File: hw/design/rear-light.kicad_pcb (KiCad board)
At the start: 2 copper layers, 65.8 x 21.8 mm, 109 parts, among them J1 Conn_ARM_SWD_TagConnect_TC203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, Q501 2N7002, Q502 2N7002, Q503 2N7002, Q601 2N7002, U300 MCP2021A-330E/SN, U400 ATSAMD21E18A-A, U500 TLD2331-3EP, U600 TLD2132-1EP, U700 BMA456

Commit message: Gen1.0 design finalization (#1)
* Final layout for Gen1.0, PCB has been ordered
* Design documentation is mostly done
* Schematic has been completed
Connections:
- net Net-(D506-A) renamed /TLD2331_OUT1a
- net Net-(D511-A) renamed /TLD2331_OUT3a
- net Net-(D511-K) renamed /TLD2331_OUT3b
- net Net-(D512-K) renamed /TLD2331_OUT3c
- net Net-(D516-A) renamed /TLD2331_OUT2a
- net Net-(D516-K) renamed /TLD2331_OUT2b
- net Net-(D517-K) renamed /TLD2331_OUT2c
- net Net-(D604-A) renamed /TLD2132_OUTa
- net Net-(D604-K) renamed /TLD2132_OUTb
- net Net-(D605-K) renamed /TLD2132_OUTc
- net Net-(Q501-G) renamed /M05_INSET1a
- net Net-(Q502-G) renamed /M05_INSET2a
- net Net-(Q503-G) renamed /M05_INSET3a
- net Net-(Q601-G) renamed /M06_INSETa
- net Net-(U500-IN_SET1) renamed /TLD2331_INSET1a
- net Net-(U500-IN_SET2) renamed /TLD2331_INSET2a
- net Net-(U500-IN_SET3) renamed /TLD2331_INSET3a
- net Net-(U600-IN_SET) renamed /TLD2132_INSETa
- D506 pad 1: Net-(D506-K) -> /TLD2331_OUT1c
- D507 pad 1: Net-(D507-K) -> /TLD2331_OUT1c
- D507 pad 2: Net-(D506-K) -> /TLD2331_OUT1c
- D508 pad 2: Net-(D507-K) -> /TLD2331_OUT1c
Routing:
- net /TLD2331_OUT1c: track 0.00 -> 30.8 mm
- net Net-(D507-K): track 15.5 -> 0.00 mm
- net Net-(D506-K): track 15.3 -> 0.00 mm

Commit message: Initial design Schematic is mostly complete
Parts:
- removed C302: 220p, Capacitor_SMD:C_0603_1608Metric
- removed C303, C304, C407, C410: 10u, Capacitor_SMD:C_0805_2012Metric
- removed C306, C408, C411, C414, C504, C602: 220n, Capacitor_SMD:C_0402_1005Metric
- removed C412: 2.2u, Capacitor_SMD:C_0805_2012Metric
- removed C509, C514, C519, C525, C607: 10n, Capacitor_SMD:C_0402_1005Metric
- removed C527, C613: 2.2n, Capacitor_SMD:C_0402_1005Metric
- removed D201, D301: SMF33CA-DIO, Diode_SMD:D_SMF
- removed D506, D507, D508, D511, D512, D513, D516, D517, D518, D604, D605, D606: LED, LED_SMD:LED_0805_2012Metric
- removed L409: 10uH, Inductor_SMD:L_0805_2012Metric
- removed Q501, Q502, Q503: 2N7002, Package_TO_SOT_SMD:SOT-23
- removed R305, R307, R413, R529, R531, R533, R536, R538, R540, R615, R619, R620, R621: 10k, Resistor_SMD:R_0402_1005Metric
- removed R403: 1k, Resistor_SMD:R_0402_1005Metric
- removed R505, R510, R515, R603: 0, Resistor_SMD:R_0603_1608Metric
- removed R520, R521, R522, R608: 18.3k, Resistor_SMD:R_0402_1005Metric
- removed R523, R609: 20k, Resistor_SMD:R_0402_1005Metric
- removed R524, R526, R528, R612, R614: 0, Resistor_SMD:R_0402_1005Metric
- removed R532: 47k, Resistor_SMD:R_0402_1005Metric
- removed R537, R539, R541, R617: 220, Resistor_SMD:R_0402_1005Metric
- removed TP1, TP10, TP11, TP12, TP13, TP14, TP15, TP16, TP2, TP20, TP21, TP22, TP23, TP3, TP4, TP5, TP6, TP7, TP8, TP9: ~, TestPoint:TestPoint_Pad_1.0x1.0mm
- removed U100: ~, Connector_JST:JST_JWPF_B04B-JWPF-SK-R_1x04_P2.00mm_Vertical
- removed U300: MCP2021A-330E/SN, Package_SO:SOIC-8_3.9x4.9mm_P1.27mm
- removed U400: ATSAMD21E18A-A, Package_QFP:TQFP-32_7x7mm_P0.8mm
- removed U500: TLD2331-3EP, Package_SO:Infineon_PG-TSDSO-14-22
- removed U600: TLD2132-1EP, Package_SO:Infineon_PG-TSDSO-14-22
- added C1: 100n, Capacitor_SMD:C_0402_1005Metric, B.Cu at (64.2, 54.5)
- added C10: 10u, Capacitor_SMD:C_0805_2012Metric, B.Cu at (76.3, 61.1)
- added C11: 22u, Capacitor_SMD:C_0805_2012Metric, B.Cu at (76.3, 64.1)
- added C12: 10u, Capacitor_SMD:C_0402_1005Metric, B.Cu at (61.4, 54.5)
- added C13: 100n, Capacitor_SMD:C_0402_1005Metric, B.Cu at (61.4, 56.5)
- added C14: 10u, Capacitor_SMD:C_0402_1005Metric, B.Cu at (61.4, 58.5)
- added C15: 100n, Capacitor_SMD:C_0402_1005Metric, B.Cu at (58.5, 54.5)
- added C16: 1u, Capacitor_SMD:C_0402_1005Metric, B.Cu at (58.5, 56.5)
- added C17: 100n, Capacitor_SMD:C_0402_1005Metric, B.Cu at (58.5, 58.5)
- added C18: 100n, Capacitor_SMD:C_0402_1005Metric, F.Cu at (137.6, 49.3)
- added C19: 100n, Capacitor_SMD:C_0402_1005Metric, F.Cu at (137.6, 51.2)
- added C2: 100u, Capacitor_SMD:CP_Elec_6.3x5.7, B.Cu at (83.4, 68.4)
- added C20: 100p, Capacitor_SMD:C_0402_1005Metric, F.Cu at (137.6, 53.2)
- added C21: 100n, Capacitor_SMD:C_0603_1608Metric, F.Cu at (146.8, 53.1)
- added C22: 10u, Capacitor_SMD:C_0805_2012Metric, F.Cu at (147.0, 50.3)
- added C23: 10n, Capacitor_SMD:C_0402_1005Metric, F.Cu at (137.6, 55.2)
- added C24: 10n, Capacitor_SMD:C_0402_1005Metric, F.Cu at (137.6, 57.1)
- added C25: 10n, Capacitor_SMD:C_0402_1005Metric, F.Cu at (140.5, 45.3)
- added C26: 10n, Capacitor_SMD:C_0402_1005Metric, F.Cu at (140.5, 47.3)
- added C27: 10n, Capacitor_SMD:C_0402_1005Metric, F.Cu at (140.5, 49.3)
- added C28: 10n, Capacitor_SMD:C_0402_1005Metric, F.Cu at (140.5, 51.2)
- added C29: 10n, Capacitor_SMD:C_0402_1005Metric, F.Cu at (140.5, 53.2)
- added C3: 2.2u, Capacitor_SMD:C_0805_2012Metric, B.Cu at (76.3, 55.0)
- added C30: 10n, Capacitor_SMD:C_0402_1005Metric, F.Cu at (140.5, 55.2)
- added C31: 10n, Capacitor_SMD:C_0402_1005Metric, F.Cu at (140.5, 57.1)
- added C32: 10n, Capacitor_SMD:C_0402_1005Metric, F.Cu at (143.3, 45.3)
- added C33: 10n, Capacitor_SMD:C_0402_1005Metric, F.Cu at (143.3, 47.3)
- added C34: 10n, Capacitor_SMD:C_0402_1005Metric, F.Cu at (143.3, 49.3)
- added C35: 10u, Capacitor_SMD:C_0402_1005Metric, F.Cu at (143.3, 51.2)
- added C36: 10u, Capacitor_SMD:C_0402_1005Metric, F.Cu at (143.3, 53.2)
- added C4: 220p, Capacitor_SMD:C_0603_1608Metric, B.Cu at (64.9, 61.2)
- added C5: 22n, Capacitor_SMD:C_0603_1608Metric, B.Cu at (64.9, 63.8)
- added C6: 100n, Capacitor_SMD:C_0402_1005Metric, F.Cu at (137.6, 45.3)
- added C7: 10n, Capacitor_SMD:C_0402_1005Metric, B.Cu at (64.2, 56.5)
- added C8: 100p, Capacitor_SMD:C_0402_1005Metric, F.Cu at (137.6, 47.3)
- added C9: 100n, Capacitor_SMD:C_0402_1005Metric, B.Cu at (64.2, 58.5)
- added D1: BAS3005B02, Diode_SMD:D_SOD-523, B.Cu at (61.0, 61.2)
- added D10: LY E6SF-ABCA-36-3B5A-50, LED_SMD:LED_Cree-PLCC4_2x2mm_CW, F.Cu at (125.0, 49.9)
- added D11: LY E6SF-ABCA-36-3B5A-50, LED_SMD:LED_Cree-PLCC4_2x2mm_CW, F.Cu at (129.5, 38.3)
- added D12: LY E6SF-ABCA-36-3B5A-50, LED_SMD:LED_Cree-PLCC4_2x2mm_CW, F.Cu at (129.5, 42.2)
- added D13: LY E6SF-ABCA-36-3B5A-50, LED_SMD:LED_Cree-PLCC4_2x2mm_CW, F.Cu at (129.5, 46.0)
- added D14: LY E6SF-ABCA-36-3B5A-50, LED_SMD:LED_Cree-PLCC4_2x2mm_CW, F.Cu at (129.5, 49.9)
- added D15: LY E6SF-ABCA-36-3B5A-50, LED_SMD:LED_Cree-PLCC4_2x2mm_CW, F.Cu at (133.9, 38.3)
- added D16: LY E6SF-ABCA-36-3B5A-50, LED_SMD:LED_Cree-PLCC4_2x2mm_CW, F.Cu at (133.9, 42.2)
- added D17: LY E6SF-ABCA-36-3B5A-50, LED_SMD:LED_Cree-PLCC4_2x2mm_CW, F.Cu at (133.9, 46.0)
- added D18: XPEBRO-L1-0000-00C01, LED_SMD:LED_Cree-XP-G, F.Cu at (72.2, 49.3)
- added D2: SS34F-DC, Diode_SMD:D_SMA, B.Cu at (65.4, 49.3)
- added D3: SDT23C15L02, Package_TO_SOT_SMD:SOT-23, B.Cu at (59.0, 44.2)
- added D5: MM5Z3V6T1G, Diode_SMD:D_SOD-523, B.Cu at (61.0, 66.1)
- added D6: LY E6SF-ABCA-36-3B5A-50, LED_SMD:LED_Cree-PLCC4_2x2mm_CW, F.Cu at (59.7, 37.9)
- added D7: LY E6SF-ABCA-36-3B5A-50, LED_SMD:LED_Cree-PLCC4_2x2mm_CW, F.Cu at (125.0, 38.3)
- added D8: LY E6SF-ABCA-36-3B5A-50, LED_SMD:LED_Cree-PLCC4_2x2mm_CW, F.Cu at (125.0, 42.2)
- added D9: LY E6SF-ABCA-36-3B5A-50, LED_SMD:LED_Cree-PLCC4_2x2mm_CW, F.Cu at (125.0, 46.0)
- added J3: Conn_ARM_SWD_TagConnect_TC2030-NL, Connector:Tag-Connect_TC2030-IDC-NL_2x03_P1.27mm_Vertical, B.Cu at (65.5, 44.5)
- added L2: 2.2u, Inductor_SMD:L_Coilcraft_LPS3010, B.Cu at (59.0, 49.3)
- added L3: 10uH, Inductor_SMD:L_0603_1608Metric, B.Cu at (64.9, 68.8)
- added Q200: SIA469DJ-T1-GE3, Package_TO_SOT_SMD:Vishay_PowerPAK_SC70-6L_Single, F.Cu at (146.8, 38.2)
- added R1: 10k, Resistor_SMD:R_0402_1005Metric, B.Cu at (85.8, 54.5)
- added R10: 0, Resistor_SMD:R_0402_1005Metric, B.Cu at (82.9, 58.5)
- added R11: 20k, Resistor_SMD:R_0402_1005Metric, B.Cu at (82.9, 60.5)
- added R12: 4.7k, Resistor_SMD:R_0402_1005Metric, B.Cu at (82.9, 62.5)
- added R13: 1k, Resistor_SMD:R_0402_1005Metric, B.Cu at (82.9, 64.5)
- added R14: 47k, Resistor_SMD:R_0402_1005Metric, B.Cu at (80.0, 54.5)
- added R15: 4.7k, Resistor_SMD:R_0402_1005Metric, B.Cu at (80.0, 56.5)
- added R16: 10k, Resistor_SMD:R_0402_1005Metric, B.Cu at (80.0, 58.5)
- added R17: 4.7k, Resistor_SMD:R_0402_1005Metric, B.Cu at (81.2, 39.7)
- added R18: 0, Resistor_SMD:R_0603_1608Metric, F.Cu at (146.8, 55.6)
- added R19: 10k, Resistor_SMD:R_0402_1005Metric, F.Cu at (137.6, 37.4)
- added R2: 10k, Resistor_SMD:R_0402_1005Metric, B.Cu at (85.8, 56.5)
- added R20: 0, Resistor_SMD:R_0402_1005Metric, F.Cu at (137.6, 39.4)
- added R200: 47k, Resistor_SMD:R_0402_1005Metric, F.Cu at (143.4, 39.4)
- added R201: 47k, Resistor_SMD:R_0402_1005Metric, F.Cu at (143.4, 41.4)
- added R21: 1k, Resistor_SMD:R_0402_1005Metric, F.Cu at (137.6, 41.4)
- added R22: 4.7k, Resistor_SMD:R_0402_1005Metric, F.Cu at (137.6, 43.3)
- added R23: 4.7k, Resistor_SMD:R_0402_1005Metric, F.Cu at (140.5, 37.4)
- added R24: 1k, Resistor_SMD:R_0402_1005Metric, F.Cu at (140.5, 39.4)
- added R25: 10k, Resistor_SMD:R_0402_1005Metric, F.Cu at (140.5, 41.4)
- added R26: 4.7k, Resistor_SMD:R_0402_1005Metric, F.Cu at (140.5, 43.3)
- added R27: 4.7k, Resistor_SMD:R_0402_1005Metric, F.Cu at (143.4, 37.4)
- added R3: 47k, Resistor_SMD:R_0402_1005Metric, B.Cu at (85.8, 58.5)
- added R4: 10k, Resistor_SMD:R_0402_1005Metric, B.Cu at (85.8, 60.5)
- added R5: 10k, Resistor_SMD:R_0402_1005Metric, B.Cu at (85.8, 62.5)
- added R6: 10k, Resistor_SMD:R_0402_1005Metric, B.Cu at (85.8, 64.5)
- added R7: 1k, Resistor_SMD:R_0402_1005Metric, B.Cu at (82.9, 54.5)
- added R8: 520m, Resistor_SMD:R_1206_3216Metric, B.Cu at (71.3, 68.9)
- added R9: 4.7k, Resistor_SMD:R_0402_1005Metric, B.Cu at (82.9, 56.5)
- added TH1: ERT-J0ER103J, Resistor_SMD:R_0402_1005Metric, F.Cu at (143.4, 43.3)
- added U1: ILD8150, Package_SO:Infineon_PG-DSO-8-27_3.9x4.9mm_EP2.65x3mm, B.Cu at (69.9, 56.8)
- added U2: MCP2003BT-E/MC, Package_DFN_QFN:DFN-8-1EP_3x2mm_P0.5mm_EP1.7x1.4mm, B.Cu at (71.5, 72.3)
- added U3: TPS629210DRLR, Package_TO_SOT_SMD:SOT-583-8, B.Cu at (76.7, 67.4)
- added U4: ~, Connector_JST:JST_JWPF_B03B-JWPF-SK-R_1x03_P2.00mm_Vertical, F.Cu at (70.4, 95.5)
- added U5: ATSAMD21E18A-MUT, Package_DFN_QFN:VQFN-32-1EP_5x5mm_P0.5mm_EP3.5x3.5mm, B.Cu at (70.5, 63.6)
- added U6: TLD7002-16ES, libs:SOP65P600X115-25N, B.Cu at (80.6, 46.9)
- added U8: XM125, libs:XM125_ACC-M, F.Cu at (72.3, 81.9)
- added U9: AP2127N-1.8, Package_TO_SOT_SMD:SOT-23, F.Cu at (147.2, 46.6)
- D200: value BAS3005B02 -> BZT52C20-TP; footprint Diode_SMD:D_SOD-523 -> Diode_SMD:D_SOD-123; moved to F.Cu
- J1: moved to F.Cu
- moved C611 59.1 mm to (202.8, 60.3)
- moved Q601 59.1 mm to (199.9, 62.8)
- moved R610 59.1 mm to (202.8, 61.6)
- moved R618 59.1 mm to (198.6, 60.1)
- moved C702 58.8 mm to (94.3, 59.6)
- moved C701 58.8 mm to (99.3, 59.0)
- moved U700 58.8 mm to (96.9, 58.7)
- moved D200 47.1 mm to (147.1, 59.8), turned to 0 degrees
- moved J1 36.7 mm to (140.2, 60.7), turned to 0 degrees
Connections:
- C611 pad 1: GND -> unconnected-(C611-Pad1)
- C611 pad 2: /TLD2132_DS -> unconnected-(C611-Pad2)
- D200 pad 1: +BATT -> VS
- D200 pad 2: VS -> Net-(D200-A)
- J1 pad 2: /M05_SWDIO -> /M07_RADAR_SWDIO
- J1 pad 3: /M05_RESET -> /~{M07_RADAR_RST}
- J1 pad 4: /M05_SWCLK -> /M07_RADAR_SWCLK
- Q601 pad 1: /M06_INSETa -> unconnected-(Q601-G-Pad1)
- Q601 pad 2: GND -> unconnected-(Q601-S-Pad2)
- Q601 pad 3: /TLD2132_INSET -> unconnected-(Q601-D-Pad3)
- R610 pad 1: GND -> unconnected-(R610-Pad1)
- R610 pad 2: /TLD2132_DS -> unconnected-(R610-Pad2)
- R618 pad 1: GND -> unconnected-(R618-Pad1)
- R618 pad 2: /M06_INSETa -> unconnected-(R618-Pad2)
- U700 pad 6: /M07_ACCEL_INT2 -> unconnected-(U700-INT2-Pad6)
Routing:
- net +3.3V: track 165.3 -> 0.00 mm, vias 9 -> 0
- net /M03_LINE: track 96.6 -> 0.00 mm, vias 1 -> 0
- net VS: track 86.8 -> 0.00 mm
- net /TLD2331_OUT2: track 58.2 -> 0.00 mm, vias 2 -> 0
- net /M05_ENABLE: track 54.8 -> 0.00 mm, vias 4 -> 0
- net /M06_ENABLE: track 49.5 -> 0.00 mm, vias 2 -> 0
- net /M05_ERROR: track 37.3 -> 0.00 mm, vias 2 -> 0
- net /M06_PWMI: track 31.4 -> 0.00 mm, vias 2 -> 0
- net /TLD2331_OUT1c: track 30.8 -> 0.00 mm
- net /M05_PWMI: track 27.1 -> 0.00 mm, vias 2 -> 0
- net /M06_ERROR: track 26.9 -> 0.00 mm, vias 2 -> 0
- net /M06_INSETa: track 25.6 -> 0.00 mm, vias 2 -> 0
- net /M05_RESET: track 19.8 -> 0.00 mm, vias 2 -> 0
- net /M03_CS: track 18.6 -> 0.00 mm, vias 2 -> 0
- net /TLD2331_OUT2c: track 16.0 -> 0.00 mm
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- removed copper zone on B.Cu, net GND
- removed copper zone on F.Cu, net GND
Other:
- board outline removed

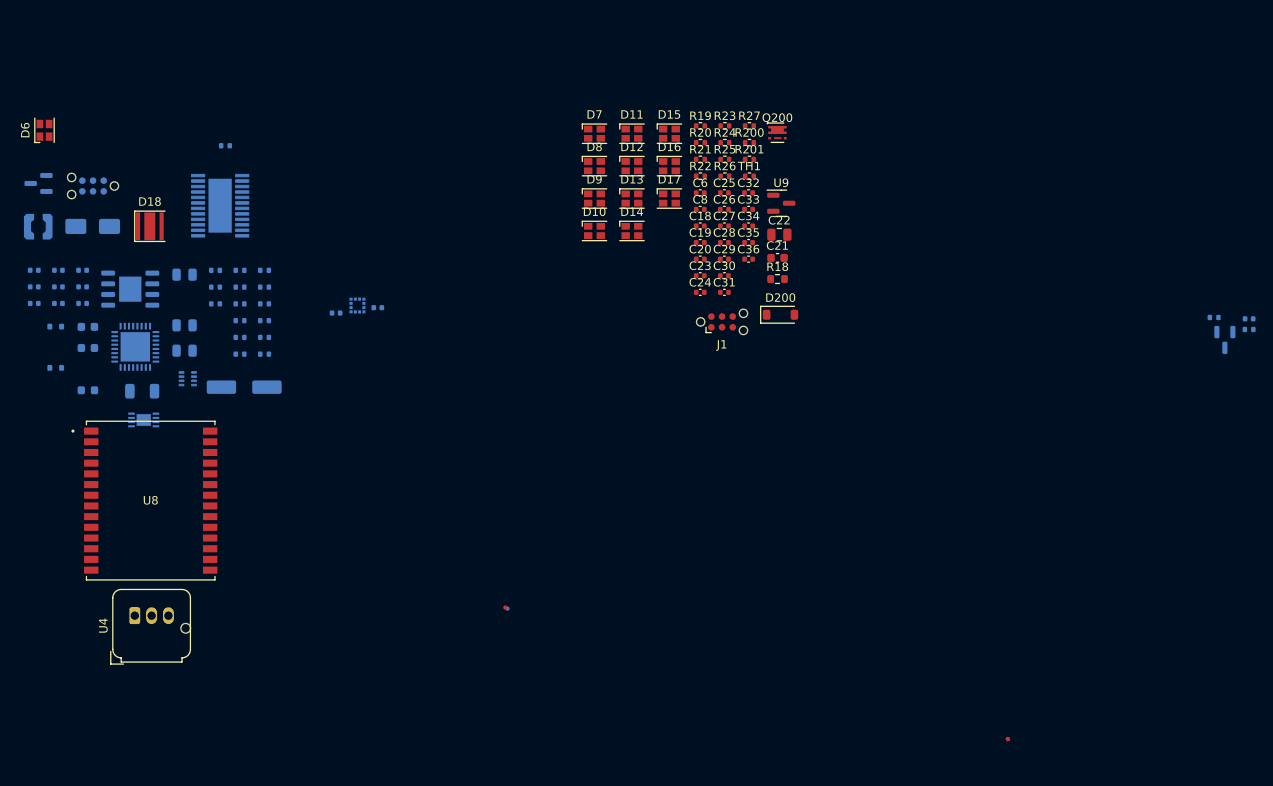
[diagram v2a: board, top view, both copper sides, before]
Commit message: Gen2.0 redesign - DCDC converter for LVIO - Voltage monitoring - Reverse polarity protection is P-FET - MCP2003 as LIN trans. - AL8891 LED driver - XM125 radar
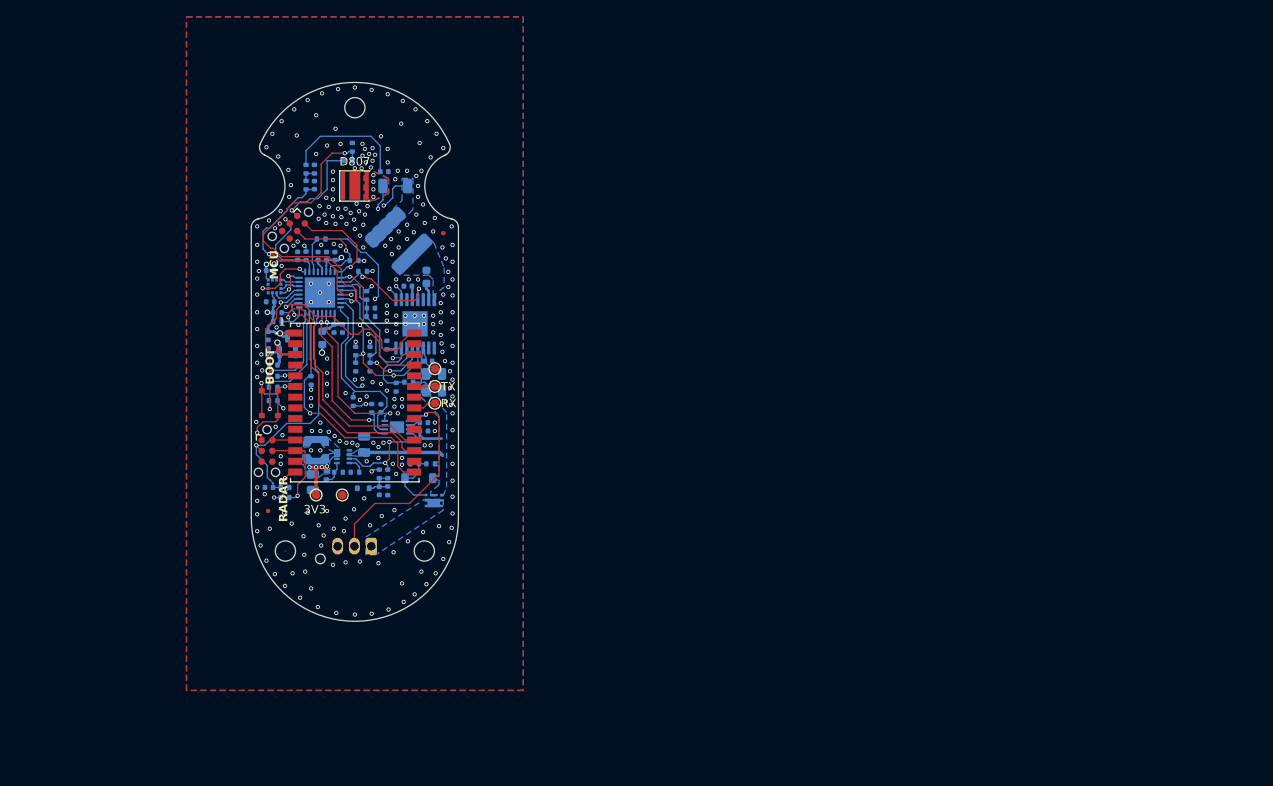
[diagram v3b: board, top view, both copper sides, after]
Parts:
- removed C1, C18: 100n, Capacitor_SMD:C_0402_1005Metric
- removed C2: 100u, Capacitor_SMD:CP_Elec_6.3x5.7
- removed C20: 100p, Capacitor_SMD:C_0402_1005Metric
- removed C21: 100n, Capacitor_SMD:C_0603_1608Metric
- removed C22: 10u, Capacitor_SMD:C_0805_2012Metric
- removed C23, C24, C25, C26, C27, C28, C29, C30, C31, C32, C33, C34, C611, C7: 10n, Capacitor_SMD:C_0402_1005Metric
- removed C3: 2.2u, Capacitor_SMD:C_0805_2012Metric
- removed C4: 220p, Capacitor_SMD:C_0603_1608Metric
- removed C5: 22n, Capacitor_SMD:C_0603_1608Metric
- removed D1: BAS3005B02, Diode_SMD:D_SOD-523
- removed D10, D11, D12, D13, D14, D15, D16, D17, D6, D7, D8, D9: LY E6SF-ABCA-36-3B5A-50, LED_SMD:LED_Cree-PLCC4_2x2mm_CW
- removed D18: XPEBRO-L1-0000-00C01, LED_SMD:LED_Cree-XP-G
- removed D2: SS34F-DC, Diode_SMD:D_SMA
- removed D3: SDT23C15L02, Package_TO_SOT_SMD:SOT-23
- removed Q601: 2N7002, Package_TO_SOT_SMD:SOT-23
- removed R17, R22, R23: 4.7k, Resistor_SMD:R_0402_1005Metric
- removed R18: 0, Resistor_SMD:R_0603_1608Metric
- removed R2, R25, R4, R5, R6, R618: 10k, Resistor_SMD:R_0402_1005Metric
- removed R20, R610: 0, Resistor_SMD:R_0402_1005Metric
- removed R24, R7: 1k, Resistor_SMD:R_0402_1005Metric
- removed R3: 47k, Resistor_SMD:R_0402_1005Metric
- removed R8: 520m, Resistor_SMD:R_1206_3216Metric
- removed TH1: ERT-J0ER103J, Resistor_SMD:R_0402_1005Metric
- removed U1: ILD8150, Package_SO:Infineon_PG-DSO-8-27_3.9x4.9mm_EP2.65x3mm
- removed U5: ATSAMD21E18A-MUT, Package_DFN_QFN:VQFN-32-1EP_5x5mm_P0.5mm_EP3.5x3.5mm
- removed U6: TLD7002-16ES, libs:SOP65P600X115-25N
- added C706: 100n, Capacitor_SMD:C_0402_1005Metric, B.Cu at (86.9, 65.8)
- added C801: 10u, Capacitor_SMD:C_0805_2012Metric, B.Cu at (106.0, 68.8)
- added C802: 2.2u, Capacitor_SMD:C_0805_2012Metric, B.Cu at (106.0, 66.8)
- added C803: 100n, Capacitor_SMD:C_0603_1608Metric, B.Cu at (105.1, 55.3)
- added C806: 100n, Capacitor_SMD:C_0402_1005Metric, B.Cu at (100.1, 42.8)
- added C808: 2.2u, Capacitor_SMD:C_0402_1005Metric, B.Cu at (102.9, 56.4)
- added C816: 10n, Capacitor_SMD:C_0402_1005Metric, B.Cu at (98.5, 59.0)
- added C826: 2.2u, Capacitor_SMD:C_0402_1005Metric, B.Cu at (91.8, 44.4)
- added C827: 100n, Capacitor_SMD:C_0402_1005Metric, B.Cu at (105.3, 65.3)
- added C902: 100n, Capacitor_SMD:C_0402_1005Metric, B.Cu at (99.5, 80.7)
- added D807: XPEBRO-L1-0000-00C01, LED_SMD:LED_Cree-XP-G, F.Cu at (96.6, 44.5)
- added L804: 22u, libs:ASPI-6045, B.Cu at (101.8, 51.0)
- added R709: 10k, Resistor_SMD:R_0402_1005Metric, B.Cu at (88.3, 80.3)
- added R712: 1.5k, Resistor_SMD:R_0402_1005Metric, B.Cu at (86.9, 67.1)
- added R713: 1.5k, Resistor_SMD:R_0402_1005Metric, B.Cu at (86.9, 68.4)
- added R717: 1.5k, Resistor_SMD:R_0402_1005Metric, B.Cu at (86.9, 70.0)
- added R718: 1.5k, Resistor_SMD:R_0402_1005Metric, B.Cu at (92.6, 50.8)
- added R805: 290m, Resistor_SMD:R_1206_3216Metric, B.Cu at (101.4, 44.5)
- added R809: 150k, Resistor_SMD:R_0402_1005Metric, B.Cu at (103.0, 67.8)
- added R810: 100k, Resistor_SMD:R_0402_1005Metric, B.Cu at (101.5, 68.4)
- added R812: 10k, Resistor_SMD:R_0402_1005Metric, B.Cu at (96.7, 64.1)
- added R813: 100k, Resistor_SMD:R_0402_1005Metric, B.Cu at (96.7, 66.0)
- added R814: 47k, Resistor_SMD:R_0402_1005Metric, B.Cu at (97.5, 54.7)
- added R815: 200k, Resistor_SMD:R_0402_1005Metric, B.Cu at (98.0, 57.5)
- added R817: 43k, Resistor_SMD:R_0402_1005Metric, B.Cu at (98.5, 60.0)
- added R818: 47k, Resistor_SMD:R_0402_1005Metric, B.Cu at (98.4, 64.1)
- added R819: 47k, Resistor_SMD:R_0402_1005Metric, B.Cu at (98.4, 66.0)
- added R820: 237k, Resistor_SMD:R_0402_1005Metric, B.Cu at (100.4, 63.4)
- added R822: 10k, Resistor_SMD:R_0402_1005Metric, B.Cu at (96.3, 39.9)
- added R823: 10k, Resistor_SMD:R_0402_1005Metric, B.Cu at (90.8, 42.5)
- added R824: 10k, Resistor_SMD:R_0402_1005Metric, B.Cu at (91.8, 42.5)
- added R825: 10k, Resistor_SMD:R_0402_1005Metric, B.Cu at (90.8, 44.4)
- added R904: 10k, Resistor_SMD:R_0402_1005Metric, B.Cu at (99.5, 78.7)
- added SW716: SW_Push, libs:KMT0, F.Cu at (86.5, 70.3)
- added TH821: ERT-J0ER103J, Resistor_SMD:R_0402_1005Metric, B.Cu at (95.8, 41.5)
- added TP400: TestPoint, TestPoint:TestPoint_Pad_D1.0mm, F.Cu at (92.0, 81.2)
- added TP401: TestPoint, TestPoint:TestPoint_Pad_D1.0mm, F.Cu at (95.1, 81.2)
- added TP700: TestPoint, TestPoint:TestPoint_Pad_D1.0mm, F.Cu at (106.1, 70.3)
- added TP701: TestPoint, TestPoint:TestPoint_Pad_D1.0mm, F.Cu at (106.1, 68.3)
- added TP702: TestPoint, TestPoint:TestPoint_Pad_D1.0mm, F.Cu at (106.1, 66.2)
- added U500: ATSAMD21E18A-M, Package_DFN_QFN:QFN-32-1EP_5x5mm_P0.5mm_EP3.6x3.6mm, B.Cu at (92.4, 57.2)
- added U800: AL8891, Package_SO:TSSOP-16-1EP_4.4x5mm_P0.65mm_EP3x3mm, B.Cu at (103.7, 60.9)
- C302: renamed from C19; moved to B.Cu
- C304: renamed from C8; moved to B.Cu
- C602: renamed from C701; value 220n -> 100n
- C603: renamed from C702; value 220n -> 100n
- C702: renamed from C35; moved to B.Cu
- C703: renamed from C36; moved to B.Cu
- C710: renamed from C6; moved to B.Cu
- D203: renamed from D200; moved to B.Cu
- J501: renamed from J3; moved to F.Cu
- Q200: moved to B.Cu
- R1: value 10k -> 4.7k
- R201: renamed from R200; value 47k -> 820k; moved to B.Cu
- R202: renamed from R201; value 47k -> 680k; moved to B.Cu
- R704: renamed from R21; moved to B.Cu
- R708: renamed from R19; moved to B.Cu
- R714: renamed from R26; value 4.7k -> 1.5k; moved to B.Cu
- R715: renamed from R27; value 4.7k -> 1.5k; moved to B.Cu
- R900: renamed from R14; value 47k -> 120k
- R901: renamed from R15; value 4.7k -> 27k
- U701: renamed from U9; moved to B.Cu
- X100: renamed from U4; moved to B.Cu
- moved FID1 90.0 mm to (107.1, 50.1)
- moved FID3 90.0 mm to (107.1, 50.1)
- moved R704 63.6 mm to (88.3, 81.5)
- moved C710 62.0 mm to (86.4, 80.3)
- moved U701 61.0 mm to (88.6, 63.3), turned to 90 degrees
- moved R715 60.7 mm to (87.4, 60.6)
- moved Q200 59.8 mm to (105.9, 81.9)
- moved C702 58.1 mm to (86.3, 62.3), turned to 90 degrees
- moved C703 58.1 mm to (86.3, 64.3), turned to -90 degrees
- moved J705 56.2 mm to (86.1, 76.0), turned to -90 degrees
- moved R714 55.6 mm to (87.4, 59.6)
- moved R708 55.2 mm to (91.4, 67.6), turned to 90 degrees
- moved R202 53.7 mm to (103.7, 77.5), turned to 180 degrees
- moved R201 53.7 mm to (105.6, 77.5), turned to 180 degrees
- moved D203 47.1 mm to (104.2, 79.2), turned to 180 degrees
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- renumbered C9 to C301, C10 to C401, C11 to C403, C14 to C504, C15 to C505, C12 to C506, C13 to C507, C16 to C508, C17 to C510, D5 to D903, J1 to J705, L2 to L402, L3 to L503, R9 to R303, R10 to R404, R11 to R405, R12 to R406, R13 to R502, R16 to R509, U2 to U300, U3 to U400, U700 to U600, U8 to U700
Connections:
- net /M03_REGEN renamed M03_REGEN
- net /M03_RXD renamed M03_RXD
- net /M03_VMON renamed /M07_VMON_RAW
- net /M07_RADAR_GPIO0 renamed M07_RADAR_GPIO1
- net /M07_RADAR_SCL renamed M07_RADAR_SCL
- net /M07_RADAR_SDA renamed M07_RADAR_SDA
- net /M07_RADAR_WAKE renamed M07_RADAR_WAKE
- net /~{M07_RADAR_RST} renamed ~{M07_RADAR_RST}
- net Net-(D200-A) renamed /M02_RPP_GATE
- C302 pad 2: /M03_EN -> M03_CS
- R1 pad 1: VCCQ -> +3.3V
- R1 pad 2: /~{M08_SHUTDOWN} -> M03_CS
- U300 pad 2: /M03_EN -> M03_CS
- U300 pad 4: /M03_TXD -> M03_TXD
- U600 pad 1: /M07_MISO -> M06_MISO
- U600 pad 10: /M07_CS_ACCEL -> M06_CS_ACCEL
- U600 pad 12: /M07_SCK -> M06_SCK
- U600 pad 2: /M07_MOSI -> M06_MOSI
- U600 pad 5: /M07_ACCEL_INT1 -> M06_INT1
- U700 pad 25: /M07_RADAR_GPIO1 -> /M07_RADAR_GPIO0a
- U700 pad 26: /M07_RADAR_BOOT -> /M07_RADAR_BOOTa
- U700 pad 28: /M07_RADAR_INT -> M07_RADAR_INT
- U700 pad 5: unconnected-(U8-UART_TX-Pad5) -> Net-(U700-UART_TX)
- U700 pad 6: unconnected-(U8-UART_RX-Pad6) -> Net-(U700-UART_RX)
- X100 pad 2: GND -> /M03_LINE
- X100 pad 3: /M03_LINE -> GND
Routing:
- net +3.3V: track 0.00 -> 50.8 mm, vias 0 -> 20
- net M08_NTC: track 0.00 -> 36.1 mm, vias 0 -> 2
- net ~{M07_RADAR_RST}: track 0.00 -> 31.9 mm, vias 0 -> 2
- net M07_RADAR_SDA: track 0.00 -> 30.9 mm, vias 0 -> 1
- net /M08_CSN: track 0.00 -> 30.1 mm, vias 0 -> 6
- net M07_RADAR_SCL: track 0.00 -> 29.9 mm, vias 0 -> 1
- net M07_RADAR_WAKE: track 0.00 -> 29.7 mm, vias 0 -> 1
- net /M07_RADAR_BOOTa: track 0.00 -> 29.2 mm, vias 0 -> 3
- net /M03_LINE: track 0.00 -> 26.6 mm, vias 0 -> 1
- net M08_LEDMON: track 0.00 -> 26.0 mm, vias 0 -> 2
- net M07_VMON: track 0.00 -> 25.9 mm, vias 0 -> 2
- net /M07_RADAR_GPIO0a: track 0.00 -> 24.3 mm, vias 0 -> 2
- net M08_ENABLE: track 0.00 -> 23.8 mm, vias 0 -> 4
- net M07_RADAR_INT: track 0.00 -> 21.7 mm, vias 0 -> 1
- net M03_CS: track 0.00 -> 21.1 mm
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- added copper zone on B.Cu, net +3.3V
- added copper zone on In2.Cu, net +3.3V
- added copper zone on B.Cu, net +BATT
- added copper zone on B.Cu, net /M08_CSN
- added copper zone on F.Cu, net /M08_CSN
- added copper zone on B.Cu, net /M08_CSP
- added copper zone on B.Cu, net /M08_SW
- added copper zone on B.Cu, net /TPS629210_SW
- added copper zone on B.Cu, net GND
- added copper zone on F.Cu, net GND
- added copper zone on In1.Cu, net GND
- added copper zone on In2.Cu, net GND
- added copper zone on B.Cu, net VS
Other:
- board outline added: 24.6 x 64 mm
- copper layers 2 -> 4
- board text added: "1"
- board text added: "3V3"
- board text added: "BOOT"
- board text added: "MCU"
- board text added: "RADAR"
- board text added: "RX"
- board text added: "TX"

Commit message: Finalized design
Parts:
- added C828: 10u, Capacitor_SMD:C_0805_2012Metric, B.Cu at (101.2, 41.1)
- D203: value BZT52C20-TP -> MM5Z20VT1G; footprint Diode_SMD:D_SOD-123 -> Diode_SMD:D_SOD-523
- D807: value XPEBRO-L1-0000-00C01 -> XPLAPR-LS-0000-00H01; footprint LED_SMD:LED_Cree-XP-G -> LED_SMD:LED_Cree-XP
- SW716: value SW_Push -> KMT071 NGJ LHS
- TP400: value TestPoint -> 3V3
- TP401, TP702: value TestPoint -> GND
- TP700: value TestPoint -> RADAR RX
- TP701: value TestPoint -> RADAR TX
- moved D203 1.04 mm to (105.2, 78.9)
- renumbered R1 to R305
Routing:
- net /M02_RPP_GATE: track 7.71 -> 4.94 mm
- net /M08_CSN: track 30.1 -> 28.9 mm
- net GND: vias 272 -> 296
